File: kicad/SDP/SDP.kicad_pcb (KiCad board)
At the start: 4 copper layers, 98 x 98 mm, 103 parts, among them J1 GPIO, J10 Limit, J11 Conn_01x07, J12 Conn_01x07, J13 Conn_01x03, J14 Conn_01x03, J15 Conn_01x03, J16 Conn_01x03, J17 Conn_01x03, J18 12V, J2 Conn_01x03, J24 POWER, J25 Conn_01x04, J26 Conn_01x02, J27 MOTOR, J3 UART, J4 I2C, J5 Conn_01x04, J6 Conn_01x04, J7 RJ25, J8 Conn_01x07, J9 Conn_01x07, SW1 SW_Push_Dual, U1 TPS54233, U2 TPS54233, U3 PIC24FJ128GA010-I/PT, U4 DS3231SN-T&R, Y1 8MHz, Y2 32.768kHz

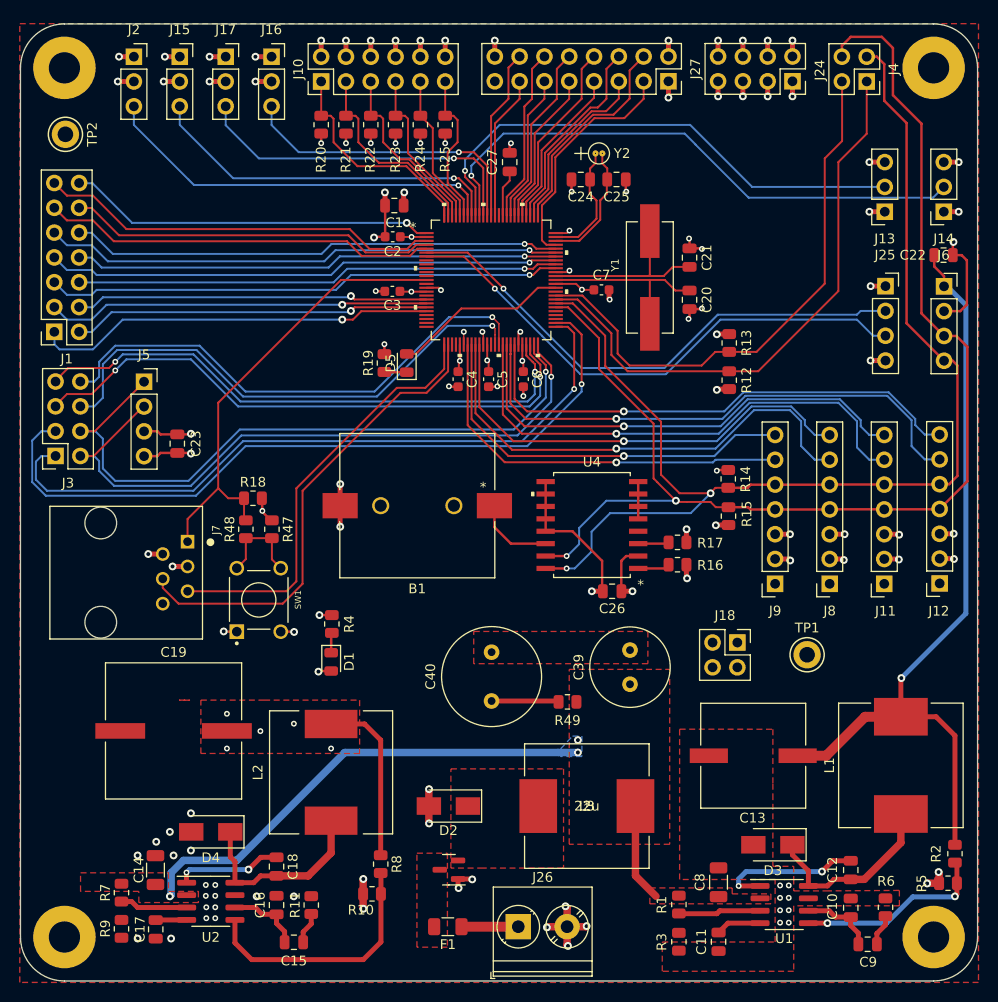
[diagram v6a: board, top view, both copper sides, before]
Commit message: Controller and motor PCB silkscreen and final layout
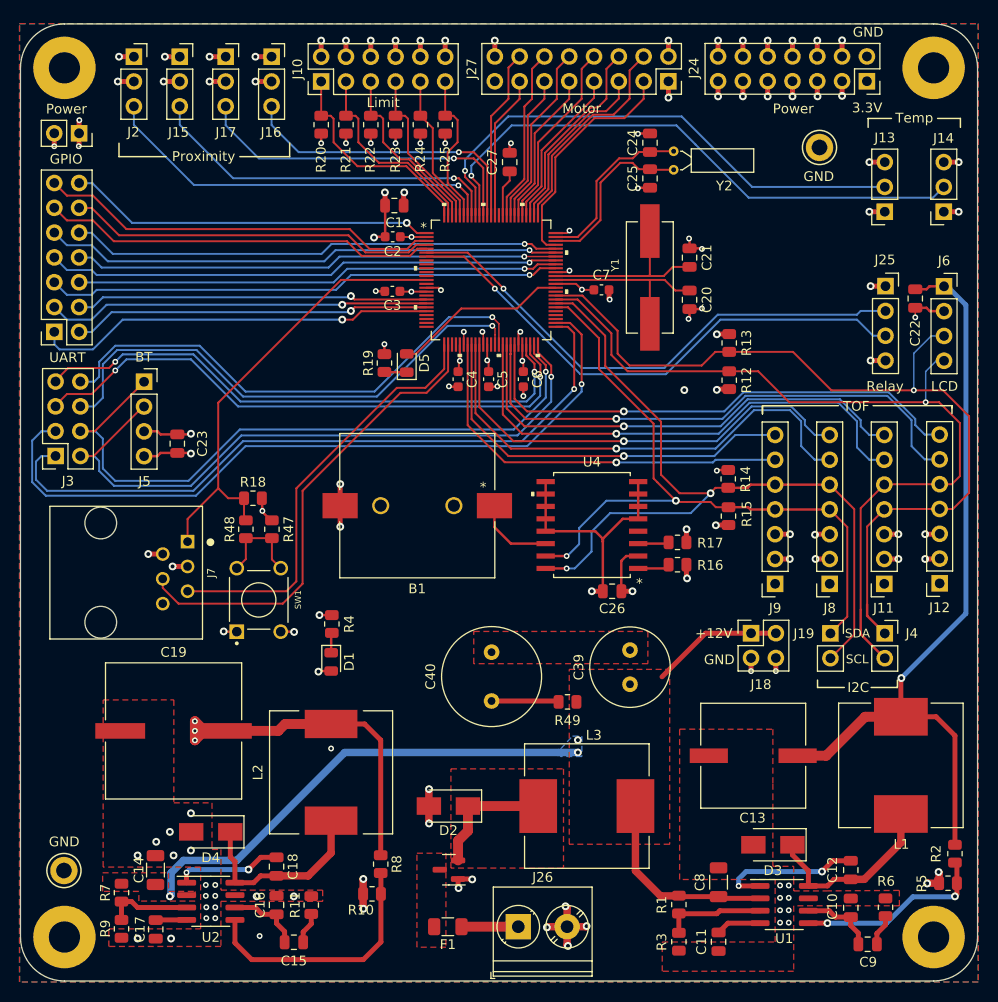
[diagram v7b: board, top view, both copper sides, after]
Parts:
- added J19: I2C2, Connector_PinSocket_2.54mm:PinSocket_1x02_P2.54mm_Vertical, F.Cu at (160.2, 106.6)
- added J20: POWER, Connector_PinSocket_2.54mm:PinSocket_1x02_P2.54mm_Vertical, F.Cu at (83.3, 55.4)
- J24: footprint Connector_PinSocket_2.54mm:PinSocket_2x04_P2.54mm_Vertical -> Connector_PinSocket_2.54mm:PinSocket_2x07_P2.54mm_Vertical
- J4: value I2C -> I2C1; footprint Connector_PinSocket_2.54mm:PinSocket_2x02_P2.54mm_Vertical -> Connector_PinSocket_2.54mm:PinSocket_1x02_P2.54mm_Vertical
- Y2: footprint CFS206:CFS206-32.768-KDZF-UB -> Crystal:Crystal_DS26_D2.0mm_L6.0mm_Horizontal
- moved TP2 75.4 mm to (81.7, 130.9)
- moved J4 56.5 mm to (165.8, 106.6), turned to 0 degrees
- moved TP1 52.0 mm to (159.1, 56.8)
- moved Y2 8.18 mm to (144.2, 59.1), turned to 90 degrees
- moved C24 8.02 mm to (141.7, 56.3), turned to 90 degrees
- moved J24 7.62 mm to (164.0, 50.0)
- moved C22 5.30 mm to (168.9, 72.3), turned to -90 degrees
- moved C25 3.43 mm to (141.7, 60.0), turned to -90 degrees
- moved J18 1.70 mm to (152.1, 106.6), turned to 90 degrees
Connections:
- J11 pad 4: P56_SDA1 -> P59_SDA2
- J11 pad 5: P57_SCL1 -> P58_SCL2
- J12 pad 4: P56_SDA1 -> P59_SDA2
- J12 pad 5: P57_SCL1 -> P58_SCL2
- J4 pad 1: P58_SCL2 -> P59_SDA2
- J4 pad 2: P57_SCL1 -> P58_SCL2
- J6 pad 3: P56_SDA1 -> P59_SDA2
- J6 pad 4: P57_SCL1 -> P58_SCL2
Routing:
- net P56_SDA1: track 129.2 -> 72.6 mm
- net P57_SCL1: track 124.1 -> 82.6 mm
- net P59_SDA2: track 57.0 -> 89.0 mm, vias 0 -> 1
- net +3V3: track 94.0 -> 123.1 mm, vias 46 -> 49
- net P58_SCL2: track 59.4 -> 86.8 mm, vias 0 -> 1
- net +12V: track 59.5 -> 83.4 mm
- net Net-(D2-Pad1): track 0.00 -> 13.2 mm
- net GND: track 128.4 -> 135.7 mm, vias 90 -> 97
- net P74_SOSCO: track 12.2 -> 17.8 mm
- net P73_SOSCI: track 12.8 -> 17.8 mm
- net Net-(R1-Pad2): track 8.45 -> 10.4 mm
- net Net-(R7-Pad2): track 6.92 -> 8.81 mm
- net P92_TEMP2: track 53.2 -> 53.9 mm
- net P91_TEMP1: track 58.3 -> 59.0 mm
- net P100_LIMIT: track 23.1 -> 22.4 mm
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- added copper zone on B.Cu, net GND
- removed copper zone on F.Cu, net +3V3
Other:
- board text added: "+12V"
- board text added: "3.3V"
- board text added: "BT"
- board text added: "GND"
- board text added: "GPIO"
- board text added: "I2C"
- board text added: "LCD"
- board text added: "Limit"
- board text added: "Motor"
- board text added: "Power"
- board text added: "Proximity"
- board text added: "Relay"
- board text added: "SCL"
- board text added: "SDA"
- board text added: "TOF"
- board text added: "Temp"
- board text added: "UART"
